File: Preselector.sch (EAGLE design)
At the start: 75 parts, among them IC58 LMZ31707RVQ, Q2 FDV303N, X1 0733660061, X2 0733660061, X3 0733660061

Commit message: Finished the 1.25m. Double check if you'd like.
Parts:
- added L6, L7, L8: 100n 1206, NewSDR:L-US1206
- added SAW_8: TA0576A, SeniorDesign:TA0576A
- added X4: 0733660061, con-coax:BU-SMA-V
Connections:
- new net 2M_RF_IN3: SAW_8.OUTPUT, X4G$1.1
- new net GND1: C23.1, L6.1, LNA_5.RF_OUT
- new net GND2: C19.1, L7.1, LNA_4.RF_OUT
- new net GND3: L8.1
- new net N$13: C27.1, L8.2, LNA_6.RF_OUT
- new net N$14: SAW_7.OUTPUT, SAW_8.INPUT
- net +5V3: now also L6.2, L7.2; no longer C19.1, C23.1, C27.1, LNA_4.RF_OUT, LNA_5.RF_OUT, LNA_6.RF_OUT
- net 1.25M_RF_IN_1: now also SAW_7.INPUT
- net GND: now also X4G$1.GND
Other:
- moved on the sheet: SAW_7
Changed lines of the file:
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@@
 <part name="IC2" library="analog-devices" deviceset="AD102" device=""/>
 <part name="IC3" library="analog-devices" deviceset="AD102" device=""/>
+<part name="L6" library="NewSDR" deviceset="L-US" device="1206" value="100n 1206"/>
+<part name="L7" library="NewSDR" deviceset="L-US" device="1206" value="100n 1206"/>
+<part name="L8" library="NewSDR" deviceset="L-US" device="1206" value="100n 1206"/>
+<part name="SAW_8" library="SeniorDesign" deviceset="TA0576A" device=""/>
+<part name="X4" library="con-coax" deviceset="BU-SMA-V" device="" value="0733660061"/>
+<part name="V4" library="supply2" deviceset="GND" device=""/>
 </parts>
 <sheets>
@@
 <text x="44.45" y="215.9" size="1.778" layer="97" rot="MR0">PRESEL IN
 TO FILTERS</text>
+<text x="171.45" y="175.26" size="1.778" layer="97" rot="MR0">PRESEL IN
+TO FILTERS</text>
 </plain>
 <instances>
@@
 <attribute name="VALUE" x="386.08" y="123.19" size="1.778" layer="96" rot="R180"/>
 </instance>
-<instance part="SAW_7" gate="G$1" x="276.86" y="157.48" smashed="yes" rot="R180">
-<attribute name="NAME" x="260.35" y="152.4" size="1.778" layer="95" rot="R180" align="center-left"/>
-<attribute name="VALUE" x="260.35" y="170.18" size="1.778" layer="96" rot="R180" align="center-left"/>
+<instance part="SAW_7" gate="G$1" x="281.94" y="160.02" smashed="yes" rot="R180">
+<attribute name="NAME" x="265.43" y="154.94" size="1.778" layer="95" rot="R180" align="center-left"/>
+<attribute name="VALUE" x="265.43" y="172.72" size="1.778" layer="96" rot="R180" align="center-left"/>
+</instance>
+<instance part="L6" gate="G$1" x="276.86" y="226.06" smashed="yes" rot="R180">
+<attribute name="NAME" x="278.13" y="231.14" size="1.778" layer="95" rot="R270"/>
+<attribute name="VALUE" x="271.78" y="234.95" size="1.778" layer="96"/>
+</instance>
+<instance part="L7" gate="G$1" x="109.22" y="228.6" smashed="yes" rot="R180">
+<attribute name="NAME" x="110.49" y="233.68" size="1.778" layer="95" rot="R270"/>
+<attribute name="VALUE" x="104.14" y="237.49" size="1.778" layer="96"/>
+</instance>
+<instance part="L8" gate="G$1" x="335.28" y="137.16" smashed="yes" rot="R180">
+<attribute name="NAME" x="336.55" y="142.24" size="1.778" layer="95" rot="R270"/>
+<attribute name="VALUE" x="330.2" y="125.73" size="1.778" layer="96"/>
+</instance>
+<instance part="SAW_8" gate="G$1" x="228.6" y="162.56" smashed="yes" rot="R180">
+<attribute name="NAME" x="212.09" y="157.48" size="1.778" layer="95" rot="R180" align="center-left"/>
+<attribute name="VALUE" x="212.09" y="175.26" size="1.778" layer="96" rot="R180" align="center-left"/>
+</instance>
+<instance part="X4" gate="G$1" x="167.64" y="167.64" smashed="yes">
+<attribute name="NAME" x="165.1" y="170.942" size="1.778" layer="95"/>
+</instance>
+<instance part="V4" gate="GND" x="170.18" y="162.56" smashed="yes" rot="MR0">
+<attribute name="VALUE" x="172.085" y="159.385" size="1.778" layer="96" rot="MR0"/>
 </instance>
 </instances>
@@
 <wire x1="368.3" y1="137.16" x2="368.3" y2="139.7" width="0.1524" layer="91"/>
 </segment>
+<segment>
+<pinref part="X4" gate="G$1" pin="GND"/>
+<pinref part="V4" gate="GND" pin="GND"/>
+</segment>
 </net>
 <net name="2M_RF_IN2" class="0">
@@
 <wire x1="90.17" y1="236.22" x2="76.2" y2="236.22" width="0.1524" layer="91"/>
 <junction x="90.17" y="236.22"/>
-<pinref part="C19" gate="G$1" pin="1"/>
-<pinref part="LNA_4" gate="G$1" pin="RF_OUT"/>
-<wire x1="101.6" y1="203.2" x2="109.22" y2="203.2" width="0.1524" layer="91"/>
-<wire x1="109.22" y1="203.2" x2="114.3" y2="203.2" width="0.1524" layer="91"/>
-<wire x1="109.22" y1="236.22" x2="109.22" y2="203.2" width="0.1524" layer="91"/>
-<junction x="109.22" y="203.2"/>
 <pinref part="+5V3" gate="G$1" pin="+5V3"/>
 <wire x1="76.2" y1="236.22" x2="60.96" y2="236.22" width="0.1524" layer="91"/>
 <wire x1="60.96" y1="236.22" x2="60.96" y2="238.76" width="0.1524" layer="91"/>
 <junction x="76.2" y="236.22"/>
+<pinref part="L7" gate="G$1" pin="2"/>
 </segment>
 <segment>
@@
 <wire x1="257.81" y1="233.68" x2="243.84" y2="233.68" width="0.1524" layer="91"/>
 <junction x="257.81" y="233.68"/>
-<pinref part="C23" gate="G$1" pin="1"/>
-<pinref part="LNA_5" gate="G$1" pin="RF_OUT"/>
-<wire x1="269.24" y1="200.66" x2="276.86" y2="200.66" width="0.1524" layer="91"/>
-<wire x1="276.86" y1="200.66" x2="281.94" y2="200.66" width="0.1524" layer="91"/>
-<wire x1="276.86" y1="233.68" x2="276.86" y2="200.66" width="0.1524" layer="91"/>
-<junction x="276.86" y="200.66"/>
 <pinref part="+5V5" gate="G$1" pin="+5V3"/>
 <wire x1="243.84" y1="233.68" x2="228.6" y2="233.68" width="0.1524" layer="91"/>
 <wire x1="228.6" y1="233.68" x2="228.6" y2="236.22" width="0.1524" layer="91"/>
 <junction x="243.84" y="233.68"/>
+<pinref part="L6" gate="G$1" pin="2"/>
 </segment>
 <segment>
@@
 <wire x1="354.33" y1="129.54" x2="368.3" y2="129.54" width="0.1524" layer="91"/>
 <junction x="354.33" y="129.54"/>
-<pinref part="C27" gate="G$1" pin="1"/>
-<pinref part="LNA_6" gate="G$1" pin="RF_OUT"/>
-<wire x1="342.9" y1="162.56" x2="335.28" y2="162.56" width="0.1524" layer="91"/>
-<wire x1="335.28" y1="162.56" x2="330.2" y2="162.56" width="0.1524" layer="91"/>
-<wire x1="335.28" y1="129.54" x2="335.28" y2="162.56" width="0.1524" layer="91"/>
-<junction x="335.28" y="162.56"/>
 <pinref part="+5V6" gate="G$1" pin="+5V3"/>
 <wire x1="368.3" y1="129.54" x2="383.54" y2="129.54" width="0.1524" layer="91"/>
@@
 <segment>
 <pinref part="C27" gate="G$1" pin="2"/>
-<wire x1="322.58" y1="162.56" x2="287.02" y2="162.56" width="0.1524" layer="91"/>
-</segment>
-</net>
+<wire x1="322.58" y1="162.56" x2="281.94" y2="162.56" width="0.1524" layer="91"/>
+<pinref part="SAW_7" gate="G$1" pin="INPUT"/>
+</segment>
+</net>
+<net name="GND1" class="1">
+<segment>
+<pinref part="L6" gate="G$1" pin="1"/>
+<junction x="276.86" y="218.44"/>
+<pinref part="C23" gate="G$1" pin="1"/>
+<pinref part="LNA_5" gate="G$1" pin="RF_OUT"/>
+<wire x1="269.24" y1="200.66" x2="276.86" y2="200.66" width="0.1524" layer="91"/>
+<wire x1="276.86" y1="200.66" x2="281.94" y2="200.66" width="0.1524" layer="91"/>
+<wire x1="276.86" y1="218.44" x2="276.86" y2="200.66" width="0.1524" layer="91"/>
+<junction x="276.86" y="200.66"/>
+</segment>
+</net>
+<net name="GND2" class="1">
+<segment>
+<pinref part="L7" gate="G$1" pin="1"/>
+<junction x="109.22" y="220.98"/>
+<pinref part="C19" gate="G$1" pin="1"/>
+<pinref part="LNA_4" gate="G$1" pin="RF_OUT"/>
+<wire x1="101.6" y1="203.2" x2="109.22" y2="203.2" width="0.1524" layer="91"/>
+<wire x1="109.22" y1="203.2" x2="114.3" y2="203.2" width="0.1524" layer="91"/>
+<wire x1="109.22" y1="220.98" x2="109.22" y2="203.2" width="0.1524" layer="91"/>
+<junction x="109.22" y="203.2"/>
+</segment>
+</net>
+<net name="N$13" class="0">
+<segment>
+<pinref part="C27" gate="G$1" pin="1"/>
+<pinref part="LNA_6" gate="G$1" pin="RF_OUT"/>
+<wire x1="342.9" y1="162.56" x2="335.28" y2="162.56" width="0.1524" layer="91"/>
+<pinref part="L8" gate="G$1" pin="2"/>
+<wire x1="335.28" y1="162.56" x2="330.2" y2="162.56" width="0.1524" layer="91"/>
+<wire x1="335.28" y1="144.78" x2="335.28" y2="162.56" width="0.1524" layer="91"/>
+<junction x="335.28" y="162.56"/>
+</segment>
+</net>
+<net name="GND3" class="1">
+<segment>
+<pinref part="L8" gate="G$1" pin="1"/>
+<junction x="335.28" y="129.54"/>
+</segment>
+</net>
+<net name="N$14" class="0">
+<segment>
+<pinref part="SAW_7" gate="G$1" pin="OUTPUT"/>
+<pinref part="SAW_8" gate="G$1" pin="INPUT"/>
+<wire x1="238.76" y1="165.1" x2="228.6" y2="165.1" width="0.1524" layer="91"/>
+</segment>
+</net>
+<net name="2M_RF_IN3" class="0">
+<segment>
+<pinref part="X4" gate="G$1" pin="1"/>
+<wire x1="170.18" y1="167.64" x2="185.42" y2="167.64" width="0.1524" layer="91"/>
+<pinref part="SAW_8" gate="G$1" pin="OUTPUT"/>
+</segment>
+</net>

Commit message: Kenneth, please check the 70cm because i think i f*ked up, jk teehee
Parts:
- removed IC1, IC2, IC3: (no value), analog-devices:AD102
- added C30, C31, C32, C36, C37, C38, C42, C43, C44: 100p 50v c0g, rcl:C-USC0603K
- added C33, C39, C45: 0.1u 16V X7R, rcl:C-USC0603K
- added C34, C35, C40, C41, C46, C47, C48, C49: 2pF, rcl:C-USC0603K
- added L10, L13, L16, L18: 86n 1206, NewSDR:L-US1206
- added L11, L14, L17, L19: 84n 1206, NewSDR:L-US1206
- added L12, L15, L9: 100n 1206, NewSDR:L-US1206
- added LNA_7, LNA_8, LNA_9: SPF-5043Z, SeniorDesign:SPF-5043Z
- added U$1, U$2, U$3, U$4: TA1914A, SeniorDesign:TA1914A
- added X5, X6: 0733660061, con-coax:BU-SMA-V
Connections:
- new net 1.25M_RF_IN2: C31.2, C34.2
- new net 1.25M_RF_IN4: C37.2, C40.2
- new net 1.25M_RF_IN5: C43.2, C46.2
- new net 2M_RF_IN10: C48.1, L18.1
- new net 2M_RF_IN11: C49.2, X6G$1.1
- new net 2M_RF_IN4: C30.1, C30.2, LNA_7.RF_IN, X5G$1.1
- new net 2M_RF_IN5: C34.1, L10.1
- new net 2M_RF_IN6: C36.2, LNA_8.RF_IN
- new net 2M_RF_IN7: C40.1, L13.1
- new net 2M_RF_IN8: C41.2, C42.1, C42.2, LNA_9.RF_IN
- new net 2M_RF_IN9: C46.1, L16.1
- new net GND4: C31.1, L9.1, LNA_7.RF_OUT
- new net GND5: C37.1, L12.1, LNA_8.RF_OUT
- new net GND6: C43.1, L15.1, LNA_9.RF_OUT
- new net N$15: C35.1, L11.2
- new net N$16: L11.1
- new net N$17: L10.2
- new net N$18: C41.1, L14.2
- new net N$19: L14.1
- new net N$20: L13.2
- new net N$21: C47.1, L17.2
- new net N$22: L17.1
- new net N$23: L16.2
- new net N$24: C49.1, L19.2
- new net N$25: L19.1
- new net N$26: L18.2
- new net N$27: C47.2, C48.2
- new net N$29: C35.2, C36.1
- net +5V3: now also C32.1, C33.1, C38.1, C39.1, C44.1, C45.1, L12.2, L15.2, L9.2
- net GND: now also C32.2, C33.2, C38.2, C39.2, C44.2, C45.2, LNA_7.GND, LNA_7.GND_1, LNA_8.GND, LNA_8.GND_1, LNA_9.GND, LNA_9.GND_1, X5G$1.GND, X6G$1.GND
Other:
- note added: "ADD INDUCTOR TO AMPLIFIER, PLEASE"

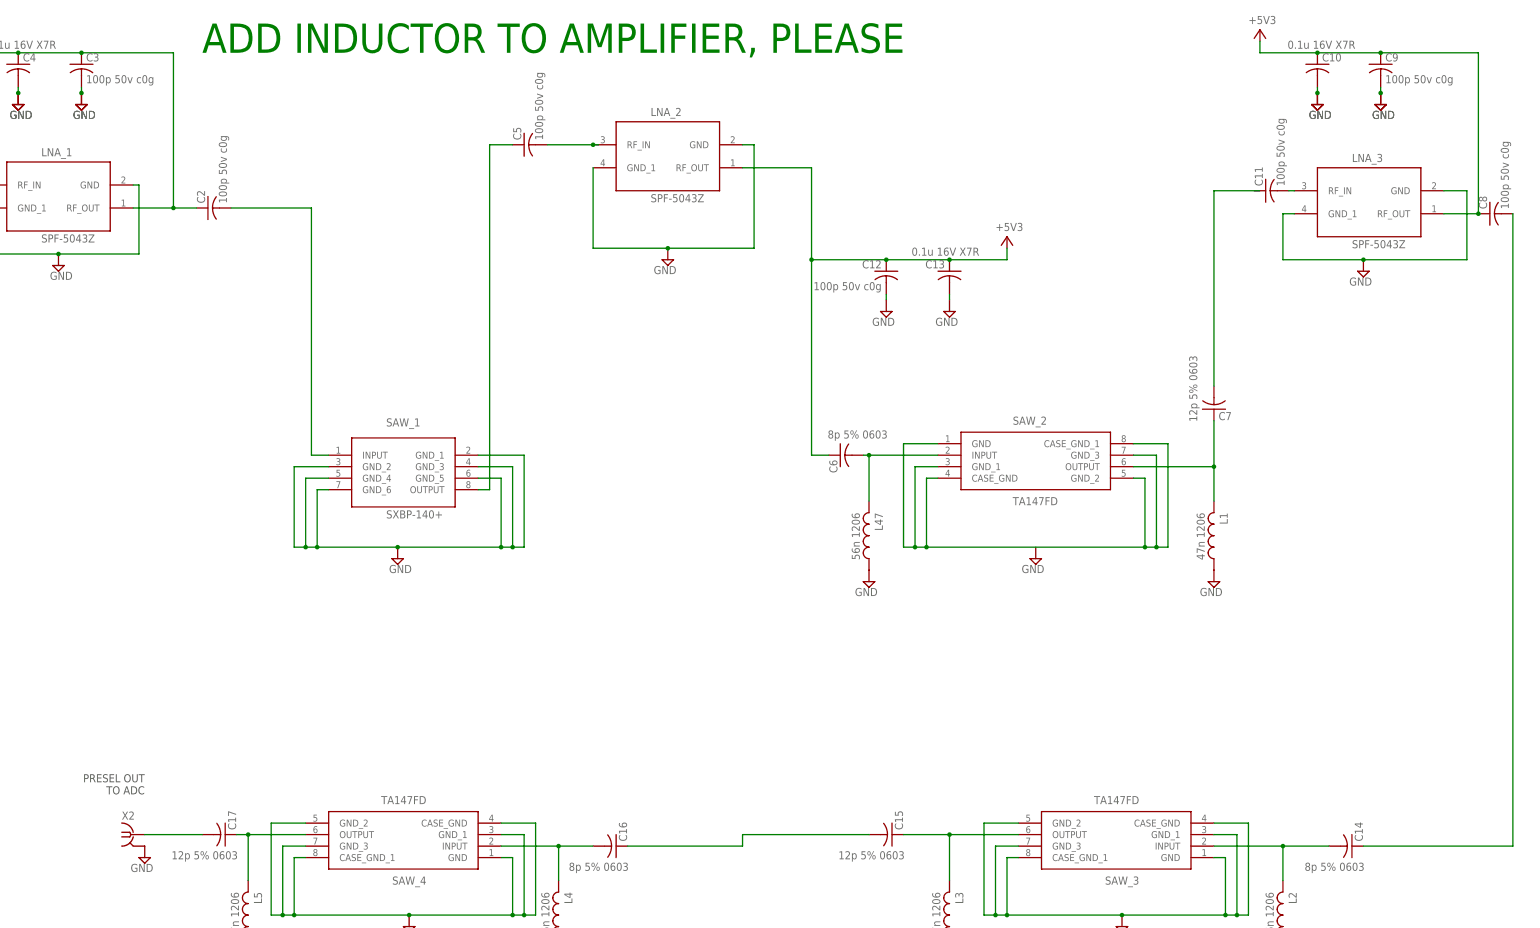
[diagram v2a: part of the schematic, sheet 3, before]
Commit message: 2m band is revised. Double check if you'd like, Kenneth.
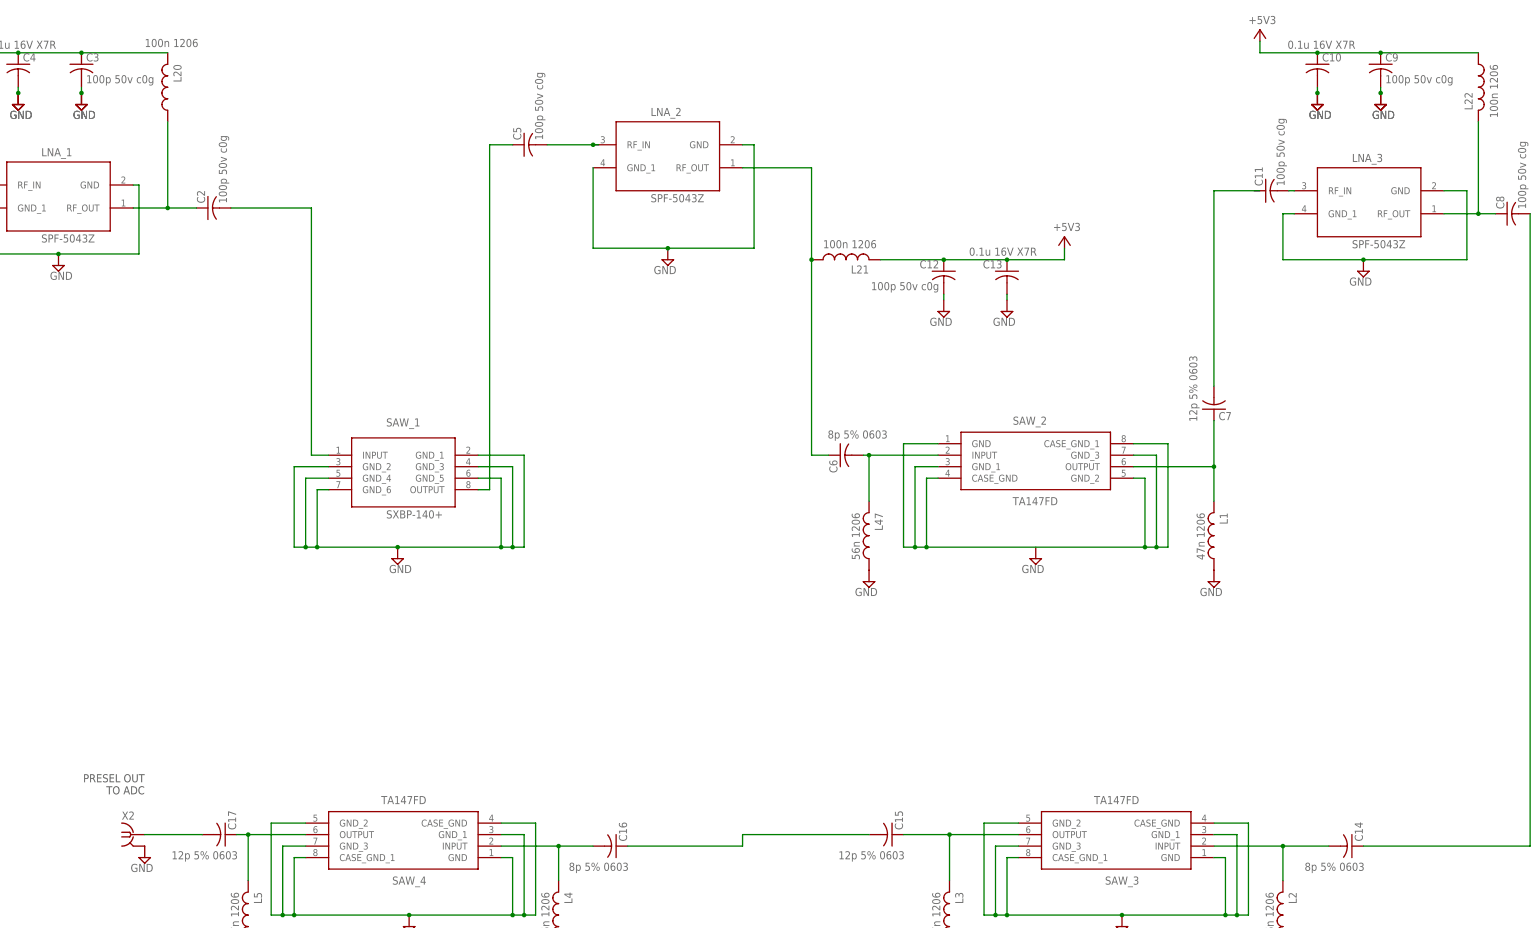
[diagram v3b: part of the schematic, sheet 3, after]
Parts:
- added L20, L21, L22: 100n 1206, NewSDR:L-US1206
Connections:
- new net N$28: C6.1, L21.1, LNA_2.RF_OUT
- new net N$30: C2.1, L20.1, LNA_1.RF_OUT
- new net N$31: C8.1, L22.2, LNA_3.RF_OUT
- net +5V3: now also L20.2, L21.2; no longer C2.1, C6.1, C8.1, LNA_1.RF_OUT, LNA_2.RF_OUT, LNA_3.RF_OUT
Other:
- note removed: "ADD INDUCTOR TO AMPLIFIER, PLEASE"
- moved on the sheet: C12, C13, C8

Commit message: Made minor changes to schematic
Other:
- note added: "1.25m Band"
- note added: "2m Band"
- note added: "70cm Band"
- note added: "This is from DECPU, there is a 5.3V output and this may be compatible, althought it does have a lot of pins that need to be soldered."
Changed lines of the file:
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@@
 <setting verticaltext="up"/>
 </settings>
-<grid distance="0.1" unitdist="inch" unit="inch" style="lines" multiple="1" display="yes" altdistance="0.01" altunitdist="inch" altunit="inch"/>
+<grid distance="0.1" unitdist="inch" unit="inch" style="lines" multiple="1" display="no" altdistance="0.01" altunitdist="inch" altunit="inch"/>
 <layers>
 <layer number="1" name="Top" color="4" fill="12" visible="no" active="no"/>
@@
 <text x="350.52" y="25.4" size="2.54" layer="94">2.04 Multiband Receive Preselector</text>
 <text x="419.1" y="7.62" size="2.54" layer="94">A</text>
+<text x="114.3" y="231.14" size="2.54" layer="106">This is from DECPU, there is a 5.3V output and this may be compatible, althought it does have a lot of pins that need to be soldered.</text>
 </plain>
 <instances>
@@
 <text x="81.28" y="95.25" size="1.778" layer="97" rot="MR0">PRESEL OUT
 TO ADC</text>
+<text x="363.22" y="25.4" size="2.54" layer="94">2m Band</text>
 </plain>
 <instances>
@@
 <text x="171.45" y="175.26" size="1.778" layer="97" rot="MR0">PRESEL IN
 TO FILTERS</text>
+<text x="360.68" y="27.94" size="2.54" layer="94">1.25m Band</text>
 </plain>
 <instances>
@@
 <text x="199.39" y="83.82" size="1.778" layer="97" rot="MR0">PRESEL IN
 TO FILTERS</text>
+<text x="363.22" y="27.94" size="2.54" layer="94">70cm Band</text>
 </plain>
 <instances>

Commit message: Cleaned up schematic and began board design
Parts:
- removed C14, C16: 8p 5% 0603, rcl:C-USC0603K
- removed C15, C17: 12p 5% 0603, rcl:C-USC0603K
- removed C20: 100p 50v c0g, rcl:C-USC0603K
- removed C21: 0.1u 16V X7R, rcl:C-USC0603K
- removed C34, C35, C40, C41, C46, C47, C48, C49: 2pF, rcl:C-USC0603K
- removed L10, L13, L16, L18: 86n 1206, NewSDR:L-US1206
- removed L11, L14, L17, L19: 84n 1206, NewSDR:L-US1206
- removed L20, L21, L22: 100n 1206, NewSDR:L-US1206
- removed L47: 56n 1206, NewSDR:L-US1206
- added C_20: 100p 50v c0g, rcl:C-USC0603K
- added C_21: 0.1u 16V X7R, rcl:C-USC0603K
- added L_00, L_7, L_8, L_9: 100n 1206, NewSDR:L-US1206
- C12, C8: value 100p 50v c0g -> 8p 5% 0603
- C13: value 0.1u 16V X7R -> 12p 5% 0603
- C2: value 100p 50v c0g -> 0.1u 16V X7R
- C4: value 0.1u 16V X7R -> 8p 5% 0603
- C5, C9: value 100p 50v c0g -> 12p 5% 0603
- C6: value 8p 5% 0603 -> 0.1u 16V X7R
- C7: value 12p 5% 0603 -> 100p 50v c0g
- L1: value 47n 1206 -> 100n 1206
- L4: value 56n 1206 -> 100n 1206
- L5: value 47n 1206 -> 56n 1206
- L6, L9: value 100n 1206 -> 47n 1206
- L8: value 100n 1206 -> 56n 1206
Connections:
- removed net 1.25M_RF_IN2: C31.2, C34.2
- removed net 1.25M_RF_IN4: C37.2, C40.2
- removed net 1.25M_RF_IN5: C43.2, C46.2
- removed net 2M_RF_IN1: X2G$1.1
- removed net 2M_RF_IN10: C48.1, L18.1
- removed net 2M_RF_IN11: C49.2, X6G$1.1
- removed net 2M_RF_IN5: C34.1, L10.1
- removed net 2M_RF_IN7: C40.1, L13.1
- removed net 2M_RF_IN9: C46.1, L16.1
- removed net N$1: C5.2, LNA_2.RF_IN
- removed net N$10: C15.2, C16.1
- removed net N$11: C16.2, L4.2, SAW_4.INPUT
- removed net N$12: C17.1, L5.2, SAW_4.OUTPUT
- removed net N$22: L17.1
- removed net N$23: L16.2
- removed net N$24: C49.1, L19.2
- removed net N$25: L19.1
- removed net N$26: L18.2
- removed net N$27: C47.2, C48.2
- removed net N$28: C6.1, L21.1, LNA_2.RF_OUT
- removed net N$29: C35.2, C36.1
- removed net N$30: C2.1, L20.1, LNA_1.RF_OUT
- removed net N$31: C8.1, L22.2, LNA_3.RF_OUT
- removed net N$4: C14.1, C8.2
- removed net N$5: C7.1, L1.2, SAW_2.OUTPUT
- removed net N$6: C11.2, LNA_3.RF_IN
- removed net N$7: SAW_2.CASE_GND, SAW_2.CASE_GND_1, SAW_2.GND, SAW_2.GND_1, SAW_2.GND_2, SAW_2.GND_3
- removed net N$8: C7.2
- removed net N$9: C15.1, L3.2, SAW_3.OUTPUT
- net +5V3: now also C11.1, C2.1, C6.1, C7.1, C_20.1, C_21.1, L1.2, L4.2, L7.1, L_00.2, L_7.2, L_9.2; no longer C12.1, C13.1, C20.1, C21.1, C4.1, C9.1, L20.2, L21.2, L6.2, L7.2, L9.2
- net 2M_RF_IN: now also C12.1, C12.2, C13.1, C4.1, C4.2, C5.2, C8.1, C9.1, C9.2, L1.1, L2.2, L3.2, L4.1, L6.2, L7.2, L8.2, L9.2, LNA_1.RF_OUT, LNA_2.RF_IN, LNA_2.RF_OUT, LNA_3.RF_IN, LNA_3.RF_OUT, SAW_2.INPUT, SAW_2.OUTPUT, SAW_3.OUTPUT, SAW_4.INPUT, SAW_4.OUTPUT; no longer C2.2
- net 2M_RF_IN8: no longer C41.2, C42.1
- net GND: now also C11.2, C2.2, C6.2, C7.2, C_20.2, C_21.2, L6.1, L8.1, L9.1, SAW_2.CASE_GND, SAW_2.CASE_GND_1, SAW_2.GND, SAW_2.GND_1, SAW_2.GND_2, SAW_2.GND_3, SAW_5.CASE_GND, SAW_5.CASE_GND_1, SAW_5.GND, SAW_5.GND_1, SAW_5.GND_2, SAW_5.GND_3, SAW_6.CASE_GND, SAW_6.CASE_GND_1, SAW_6.GND, SAW_6.GND_1, SAW_6.GND_2, SAW_6.GND_3, SAW_7.CASE_GND, SAW_7.CASE_GND_1, SAW_7.GND, SAW_7.GND_1, SAW_7.GND_2, SAW_7.GND_3, SAW_8.CASE_GND, SAW_8.CASE_GND_1, SAW_8.GND, SAW_8.GND_1, SAW_8.GND_2, SAW_8.GND_3, U$1.GND, U$1.GND_1, U$1.GND_2, U$1.GND_3, U$2.GND, U$2.GND_1, U$2.GND_2, U$2.GND_3, U$3.GND, U$3.GND_1, U$3.GND_2, U$3.GND_3, U$4.GND, U$4.GND_1, U$4.GND_2, U$4.GND_3; no longer C12.2, C13.2, C20.2, C21.2, C4.2, C9.2, L1.1, L4.1, L47.1
- net GND1: now also L_00.1; no longer L6.1
- net GND2: now also L_7.1; no longer L7.1
- net GND3: now also L_8.1; no longer L8.1
- net GND4: now also L_9.1; no longer L9.1
- net N$13: now also L_8.2; no longer L8.2
- net N$15: now also C31.2, U$1.INPUT; no longer C35.1, L11.2
- net N$16: now also C36.1, U$1.OUTPUT; no longer L11.1
- net N$17: now also C37.2, U$2.INPUT; no longer L10.2
- net N$18: now also C42.1, U$2.OUTPUT; no longer C41.1, L14.2
- net N$19: now also C43.2, U$3.INPUT; no longer L14.1
- net N$2: now also C13.2, X2G$1.1; no longer C6.2, L47.2, SAW_2.INPUT
- net N$20: now also U$3.OUTPUT, U$4.OUTPUT; no longer L13.2
- net N$21: now also U$4.INPUT, X6G$1.1; no longer C47.1, L17.2
- net N$3: now also C8.2, L5.2; no longer C14.2, L2.2
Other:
- moved on the sheet: C1, C10, C11, C12, C13, C18, C19, C2, C22, C23, C24, C25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
